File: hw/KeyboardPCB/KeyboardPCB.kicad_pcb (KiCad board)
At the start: 2 copper layers, 335 x 100 mm, 164 parts, among them IC1 TPS2113ADRBR, IC2 BGM220PC22HNA2R, J1 USB_B_Micro, J2 Conn_01x07_Pin, J3 Conn_01x06_Pin, J4 Conn_02x05_Odd_Even, J5 BATT_POS, J6 BATT_NEG, K1 KEYSW, K10 KEYSW, K11 KEYSW, K12 KEYSW, K13 KEYSW, K14 KEYSW, K15 KEYSW, K16 KEYSW, K17 KEYSW, K18 KEYSW, K19 KEYSW, K2 KEYSW, K20 KEYSW, K21 KEYSW, K22 KEYSW, K23 KEYSW, K24 KEYSW, K25 KEYSW, K26 KEYSW, K27 KEYSW, K28 KEYSW, K29 KEYSW, K3 KEYSW, K30 KEYSW, K31 KEYSW, K32 KEYSW, K33 KEYSW, K34 KEYSW, K35 KEYSW, K36 KEYSW, K37 KEYSW, K38 KEYSW, K39 KEYSW, K4 KEYSW, K40 KEYSW, K41 KEYSW, K42 KEYSW, K43 KEYSW, K44 KEYSW, K45 KEYSW, K46 KEYSW, K47 KEYSW, K48 KEYSW, K49 KEYSW, K5 KEYSW, K50 KEYSW, K51 KEYSW, K52 KEYSW, K53 KEYSW, K54 KEYSW, K55 KEYSW, K56 KEYSW, K57 KEYSW, K58 KEYSW, K59 KEYSW, K6 KEYSW, K60 KEYSW, K61 KEYSW, K62 KEYSW, K7 KEYSW, K8 KEYSW, K9 KEYSW, SW2 BAT_SWITCH, U1 TM4C123GH6PMI7, U2 TPS73633DBV, U3 Adafruit ST7735R, X2 16MHz

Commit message: Updated BoM to include LEDs and M2x4 mounting screws.
Length of screws can be updated depending on the thickness of the PCB

Also updated resistor values based on forward voltage of SMD LEDs
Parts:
- D20, D71, D9: footprint LED_THT:LED_D5.0mm -> LED_SMD:LED_0603_1608Metric_Pad1.05x0.95mm_HandSolder
- R10, R6, R9: value 1.6k -> 1.1k
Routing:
- net /3V3: track 200.3 -> 201.5 mm
- net GND: track 207.6 -> 206.7 mm
- net Net-(D71-A): track 4.03 -> 4.72 mm
- net Net-(D9-K): track 2.11 -> 2.62 mm, vias 0 -> 1
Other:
- outline, holes or cut-outs redrawn

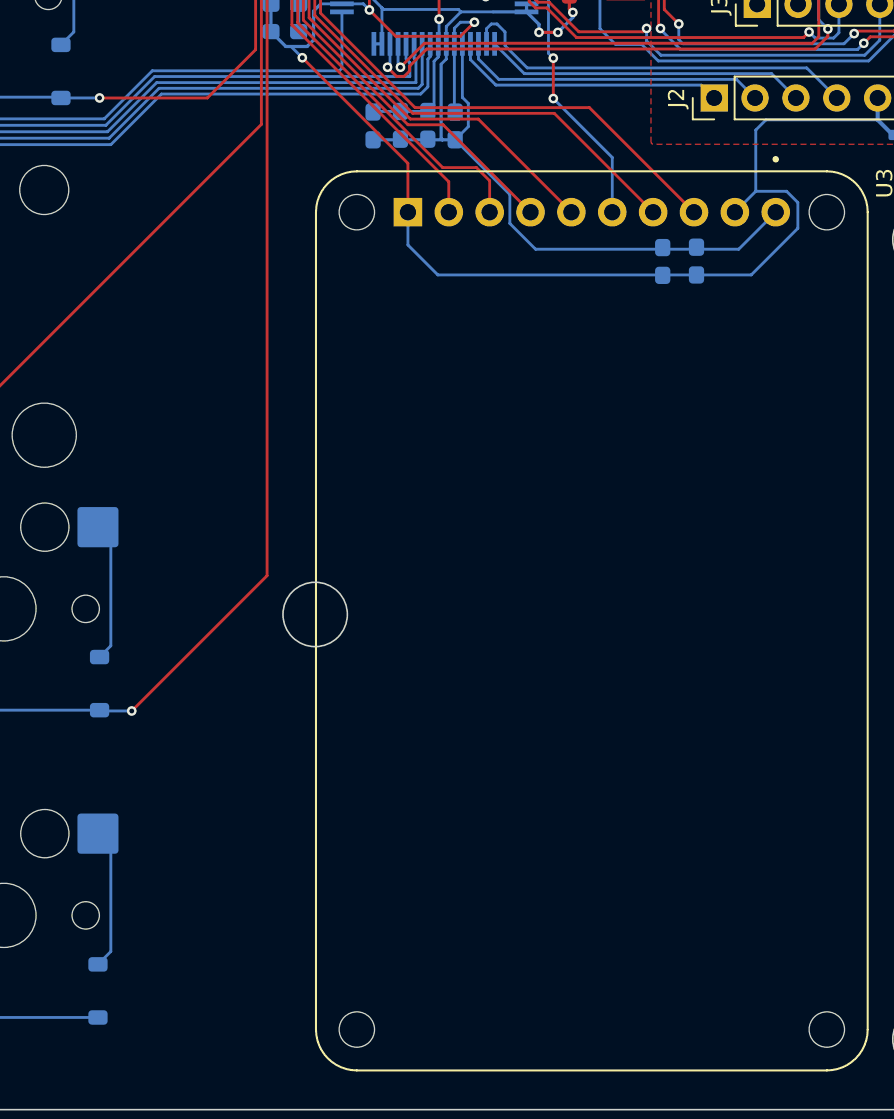
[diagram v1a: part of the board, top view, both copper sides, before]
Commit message: Routed row4 to JTAG_TDO
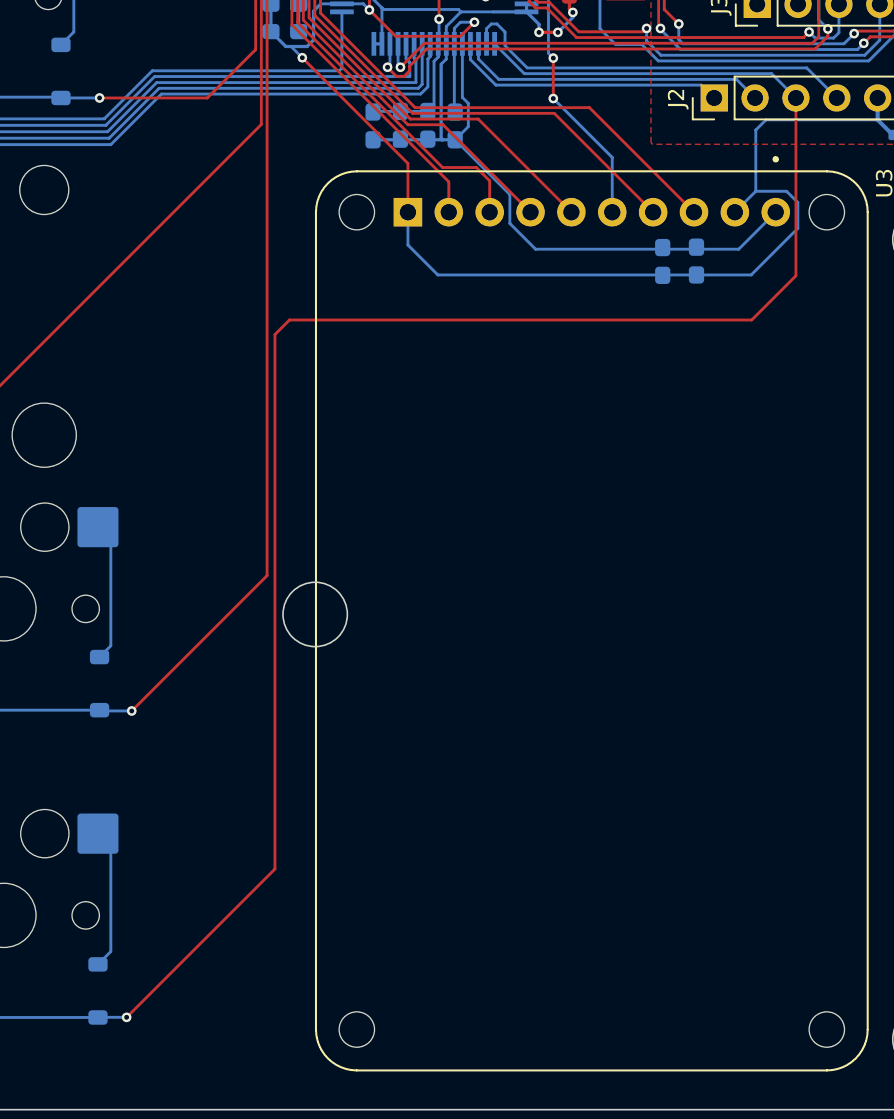
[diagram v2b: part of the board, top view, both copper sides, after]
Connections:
- D10 pad 2: /row4 -> /JTAG_SWO_TDO
- D15 pad 2: /row4 -> /JTAG_SWO_TDO
- D30 pad 2: /row4 -> /JTAG_SWO_TDO
- D5 pad 2: /row4 -> /JTAG_SWO_TDO
- D50 pad 2: /row4 -> /JTAG_SWO_TDO
- D55 pad 2: /row4 -> /JTAG_SWO_TDO
- D60 pad 2: /row4 -> /JTAG_SWO_TDO
- D65 pad 2: /row4 -> /JTAG_SWO_TDO
- J1 pad 2: /USB_D- -> Net-(J1-D-)
- J1 pad 3: /USB_D+ -> Net-(J1-D+)
- U1 pad 43: /USB_D- -> Net-(U1-PD4)
- U1 pad 44: /USB_D+ -> Net-(U1-PD5)
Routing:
- net /JTAG_SWO_TDO: track 20.1 -> 376.6 mm, vias 0 -> 1
- net /row4: track 263.5 -> 0.00 mm
- net (no net): track 0.00 -> 74.6 mm, vias 0 -> 2
- net /USB_D+: track 37.7 -> 0.00 mm, vias 1 -> 0
- net /USB_D-: track 36.9 -> 0.00 mm, vias 1 -> 0
